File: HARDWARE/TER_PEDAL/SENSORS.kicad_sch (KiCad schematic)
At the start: 0 parts

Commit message: Added Sensors PSU
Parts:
- added C12 (x4): 10u, symbol Device:C
- added U3 (x2): LM1117MP-3.3, Package_TO_SOT_SMD:SOT-223-3_TabPin2, symbol Regulator_Linear:LM1117MP-3.3
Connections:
- new net: C12.1, U3.2 (VO) (x2)
- new net +5V: C12.1, C12.1, U3.3 (VI), U3.3 (VI)
- new net GND: C12.2, C12.2, C12.2, C12.2, U3.1 (GND), U3.1 (GND)

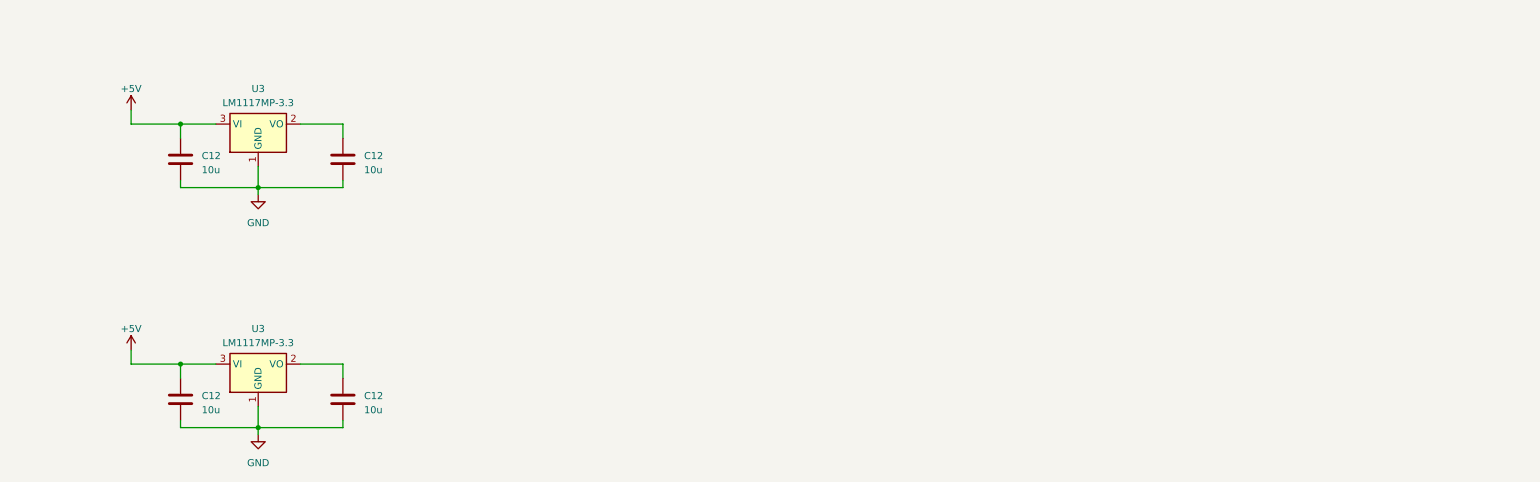
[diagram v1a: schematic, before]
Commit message: Added footprints to existing components
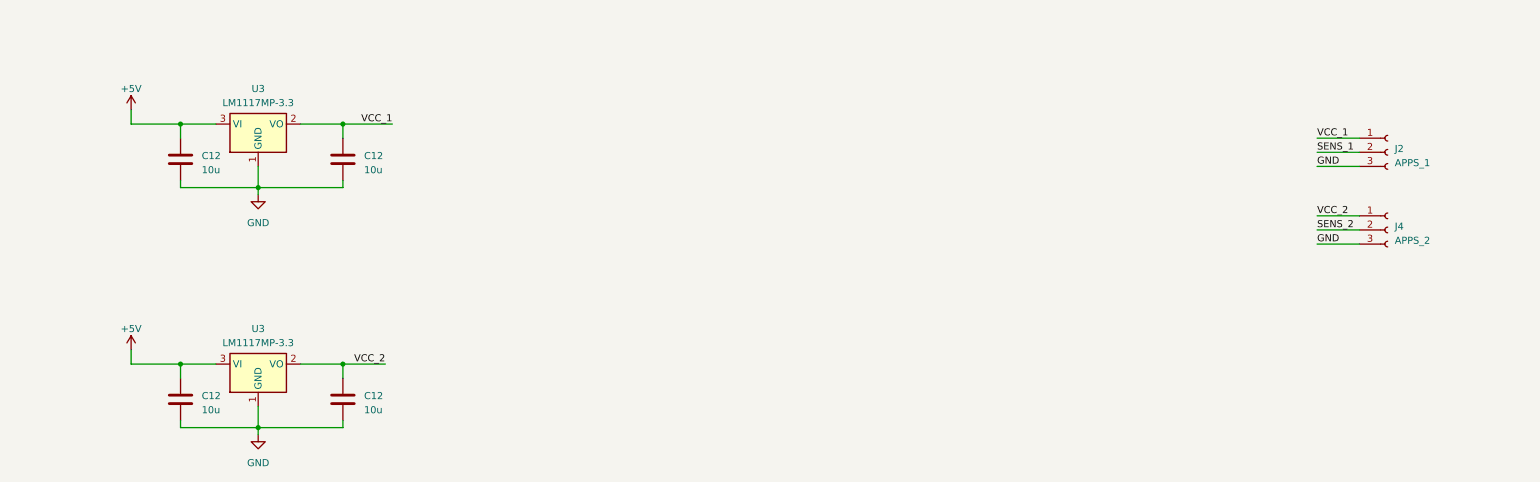
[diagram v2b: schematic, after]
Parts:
- added J2: APPS_1, Connector_Phoenix_MC:PhoenixContact_MCV_1,5_3-GF-3.5_1x03_P3.50mm_Vertical_ThreadedFlange_MountHole, symbol Connector:Conn_01x03_Female
- added J4: APPS_2, Connector_Phoenix_MC:PhoenixContact_MCV_1,5_3-GF-3.5_1x03_P3.50mm_Vertical_ThreadedFlange_MountHole, symbol Connector:Conn_01x03_Female
- C12: footprint (none) -> Capacitor_SMD:C_0603_1608Metric
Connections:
- net GND: now also J2.3 (Pin_3), J4.3 (Pin_3)
- net VCC_1: now reaches C12.1, U3.2 (VO)
- net VCC_1: now also J2.1 (Pin_1)
- net VCC_2: now reaches C12.1, U3.2 (VO)
- net VCC_2: now also J4.1 (Pin_1)
- new net SENS_1: J2.2 (Pin_2)
- new net SENS_2: J4.2 (Pin_2)
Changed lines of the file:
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@@
   (junction (at 41.91 33.02) (diameter 0) (color 0 0 0 0)
   )
+  (junction (at 71.12 76.2) (diameter 0) (color 0 0 0 0)
+  )
   (junction (at 41.91 76.2) (diameter 0) (color 0 0 0 0)
   )
   (junction (at 55.88 44.45) (diameter 0) (color 0 0 0 0)
   )
+  (junction (at 71.12 33.02) (diameter 0) (color 0 0 0 0)
+  )
   (junction (at 55.88 87.63) (diameter 0) (color 0 0 0 0)
   )
@@
     (stroke (width 0) (type default))
   )
+  (wire (pts (xy 246.38 35.56) (xy 254 35.56))
+    (stroke (width 0) (type default))
+  )
   (wire (pts (xy 41.91 76.2) (xy 33.02 76.2))
     (stroke (width 0) (type default))
@@
     (stroke (width 0) (type default))
   )
+  (wire (pts (xy 71.12 33.02) (xy 80.01 33.02))
+    (stroke (width 0) (type default))
+  )
   (wire (pts (xy 71.12 44.45) (xy 55.88 44.45))
     (stroke (width 0) (type default))
@@
     (stroke (width 0) (type default))
   )
+  (wire (pts (xy 246.38 54.61) (xy 254 54.61))
+    (stroke (width 0) (type default))
+  )
+  (wire (pts (xy 246.38 52.07) (xy 254 52.07))
+    (stroke (width 0) (type default))
+  )
+  (wire (pts (xy 246.38 40.64) (xy 254 40.64))
+    (stroke (width 0) (type default))
+  )
   (wire (pts (xy 41.91 86.36) (xy 41.91 87.63))
     (stroke (width 0) (type default))
@@
     (stroke (width 0) (type default))
   )
+  (wire (pts (xy 246.38 38.1) (xy 254 38.1))
+    (stroke (width 0) (type default))
+  )
   (wire (pts (xy 71.12 86.36) (xy 71.12 87.63))
     (stroke (width 0) (type default))
@@
     (stroke (width 0) (type default))
   )
+  (wire (pts (xy 71.12 76.2) (xy 78.74 76.2))
+    (stroke (width 0) (type default))
+  )
   (wire (pts (xy 63.5 76.2) (xy 71.12 76.2))
     (stroke (width 0) (type default))
   )
+  (wire (pts (xy 246.38 49.53) (xy 254 49.53))
+    (stroke (width 0) (type default))
+  )
   (wire (pts (xy 55.88 88.9) (xy 55.88 87.63))
     (stroke (width 0) (type default))
   )
+  (label "SENS_1" (at 246.38 38.1 0) (fields_autoplaced)
+    (effects (font (size 1.27 1.27)) (justify left bottom))
+  )
+  (label "VCC_2" (at 246.38 49.53 0) (fields_autoplaced)
+    (effects (font (size 1.27 1.27)) (justify left bottom))
+  )
+  (label "VCC_1" (at 246.38 35.56 0) (fields_autoplaced)
+    (effects (font (size 1.27 1.27)) (justify left bottom))
+  )
+  (label "VCC_2" (at 78.74 76.2 180) (fields_autoplaced)
+    (effects (font (size 1.27 1.27)) (justify right bottom))
+  )
+  (label "SENS_2" (at 246.38 52.07 0) (fields_autoplaced)
+    (effects (font (size 1.27 1.27)) (justify left bottom))
+  )
+  (label "GND" (at 246.38 54.61 0) (fields_autoplaced)
+    (effects (font (size 1.27 1.27)) (justify left bottom))
+  )
+  (label "VCC_1" (at 80.01 33.02 180) (fields_autoplaced)
+    (effects (font (size 1.27 1.27)) (justify right bottom))
+  )
+  (label "GND" (at 246.38 40.64 0) (fields_autoplaced)
+    (effects (font (size 1.27 1.27)) (justify left bottom))
+  )
   (symbol (lib_id "Device:C") (at 71.12 39.37 0) (unit 1)
     (in_bom yes) (on_board yes) (dnp no) (fields_autoplaced)
@@
       (effects (font (size 1.27 1.27)) (justify left))
     )
-    (property "Footprint" "" (at 72.0852 43.18 0)
+    (property "Footprint" "Capacitor_SMD:C_0603_1608Metric" (at 72.0852 43.18 0)
       (effects (font (size 1.27 1.27)) hide)
     )
@@
       (effects (font (size 1.27 1.27)) (justify left))
     )
-    (property "Footprint" "" (at 42.8752 86.36 0)
+    (property "Footprint" "Capacitor_SMD:C_0603_1608Metric" (at 42.8752 86.36 0)
       (effects (font (size 1.27 1.27)) hide)
     )
@@
       (effects (font (size 1.27 1.27)) (justify left))
     )
-    (property "Footprint" "" (at 72.0852 86.36 0)
+    (property "Footprint" "Capacitor_SMD:C_0603_1608Metric" (at 72.0852 86.36 0)
       (effects (font (size 1.27 1.27)) hide)
     )
@@
       (effects (font (size 1.27 1.27)) (justify left))
     )
-    (property "Footprint" "" (at 42.8752 43.18 0)
+    (property "Footprint" "Capacitor_SMD:C_0603_1608Metric" (at 42.8752 43.18 0)
       (effects (font (size 1.27 1.27)) hide)
     )
@@
         )
       )
+    )
+  )
+  (symbol (lib_id "Connector:Conn_01x03_Female") (at 259.08 38.1 0) (unit 1)
+    (in_bom yes) (on_board yes) (dnp no) (fields_autoplaced)
+    (property "Reference" "J2" (at 260.35 37.465 0)
+      (effects (font (size 1.27 1.27)) (justify left))
+    )
+    (property "Value" "APPS_1" (at 260.35 40.005 0)
+      (effects (font (size 1.27 1.27)) (justify left))
+    )
+    (property "Footprint" "Connector_Phoenix_MC:PhoenixContact_MCV_1,5_3-GF-3.5_1x03_P3.50mm_Vertical_ThreadedFlange_MountHole" (at 259.08 38.1 0)
+      (effects (font (size 1.27 1.27)) hide)
+    )
+    (property "Datasheet" "~" (at 259.08 38.1 0)
+      (effects (font (size 1.27 1.27)) hide)
+    )
+    (pin "1")
+    (pin "2")
+    (pin "3")
+    (instances
+      (project "TER_PEDAL"
+        (path "/73ede3a3-6344-40fe-9207-10ff50d388ba/bd370b0f-91e5-4328-9d6f-8dc10ff0cff7"
+          (reference "J2") (unit 1)
+        )
+      )
+    )
+  )
+  (symbol (lib_id "Connector:Conn_01x03_Female") (at 259.08 52.07 0) (unit 1)
+    (in_bom yes) (on_board yes) (dnp no) (fields_autoplaced)
+    (property "Reference" "J4" (at 260.35 51.435 0)
+      (effects (font (size 1.27 1.27)) (justify left))
+    )
+    (property "Value" "APPS_2" (at 260.35 53.975 0)
+      (effects (font (size 1.27 1.27)) (justify left))
+    )
+    (property "Footprint" "Connector_Phoenix_MC:PhoenixContact_MCV_1,5_3-GF-3.5_1x03_P3.50mm_Vertical_ThreadedFlange_MountHole" (at 259.08 52.07 0)
+      (effects (font (size 1.27 1.27)) hide)
+    )
+    (property "Datasheet" "~" (at 259.08 52.07 0)
+      (effects (font (size 1.27 1.27)) hide)
+    )
+    (pin "1")
+    (pin "2")
+    (pin "3")
+    (instances
+      (project "TER_PEDAL"
+        (path "/73ede3a3-6344-40fe-9207-10ff50d388ba/bd370b0f-91e5-4328-9d6f-8dc10ff0cff7"
+          (reference "J4") (unit 1)
+        )
+      )

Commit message: Finished Initial Schematic
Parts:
- added C23: 10u, Capacitor_SMD:C_0603_1608Metric, symbol Device:C_Small
- added J5: APPS_1, Connector_Phoenix_MC:PhoenixContact_MCV_1,5_3-GF-3.5_1x03_P3.50mm_Vertical_ThreadedFlange_MountHole, symbol Connector:Conn_01x03_Female
- added R10: 2k, Resistor_SMD:R_0603_1608Metric, symbol Device:R
- added R11: 4.7k, Resistor_SMD:R_0603_1608Metric, symbol Device:R
- added R12: 9.1k, Resistor_SMD:R_0603_1608Metric, symbol Device:R
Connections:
- net +5V: now also C23.1, J5.1 (Pin_1)
- net GND: now also C23.2, J5.3 (Pin_3), R12.2
- net SENS_2: now also R10.2
- net SENS_1 renamed APPS_1
- new net APPS_2: R10.1
- new net BPPS: R11.2, R12.1
- new net Brake: J5.2 (Pin_2), R11.1
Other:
- note added: "5v -> 3v signal sifter"
- note added: "APPS Connections"
- note added: "Brake Pedal Position Sensor BPPS"
- note added: "Este resistor está para inclinar la función de transferencia del APPS_2 y que no coincida con la del APPS_1 cambiar por un 0R si se quiere hacer bypass"
- note added: "Independent APPS PSU"
- moved on the sheet: C12, J2, J4, U3

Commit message: Started Layout and fixed wrong footprints
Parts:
- J2, J4: footprint Connector_Phoenix_MC:PhoenixContact_MCV_1,5_3-GF-3.5_1x03_P3.50mm_Vertical_ThreadedFlange_MountHole -> Connector_Wuerth:Wuerth_WR-WTB_64800311622_1x03_P1.50mm_Vertical
- J5: value APPS_1 -> BPPS_1; footprint Connector_Phoenix_MC:PhoenixContact_MCV_1,5_3-GF-3.5_1x03_P3.50mm_Vertical_ThreadedFlange_MountHole -> Connector_Wuerth:Wuerth_WR-WTB_64800311622_1x03_P1.50mm_Vertical
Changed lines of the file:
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@@
       (effects (font (size 1.27 1.27)) (justify left))
     )
-    (property "Footprint" "Connector_Phoenix_MC:PhoenixContact_MCV_1,5_3-GF-3.5_1x03_P3.50mm_Vertical_ThreadedFlange_MountHole" (at 166.37 34.29 0)
+    (property "Footprint" "Connector_Wuerth:Wuerth_WR-WTB_64800311622_1x03_P1.50mm_Vertical" (at 166.37 34.29 0)
       (effects (font (size 1.27 1.27)) hide)
     )
@@
       (effects (font (size 1.27 1.27)) (justify left))
     )
-    (property "Footprint" "Connector_Phoenix_MC:PhoenixContact_MCV_1,5_3-GF-3.5_1x03_P3.50mm_Vertical_ThreadedFlange_MountHole" (at 166.37 48.26 0)
+    (property "Footprint" "Connector_Wuerth:Wuerth_WR-WTB_64800311622_1x03_P1.50mm_Vertical" (at 166.37 48.26 0)
       (effects (font (size 1.27 1.27)) hide)
     )
@@
       (effects (font (size 1.27 1.27)) (justify left))
     )
-    (property "Value" "APPS_1" (at 273.05 48.895 0)
+    (property "Value" "BPPS_1" (at 273.05 48.895 0)
       (effects (font (size 1.27 1.27)) (justify left))
     )
-    (property "Footprint" "Connector_Phoenix_MC:PhoenixContact_MCV_1,5_3-GF-3.5_1x03_P3.50mm_Vertical_ThreadedFlange_MountHole" (at 271.78 46.99 0)
+    (property "Footprint" "Connector_Wuerth:Wuerth_WR-WTB_64800311622_1x03_P1.50mm_Vertical" (at 271.78 46.99 0)
       (effects (font (size 1.27 1.27)) hide)
     )

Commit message: Added Eracing Logo
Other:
- note added: "Brake Pedal Pressure Sensor BPPS"
- note removed: "Brake Pedal Position Sensor BPPS"
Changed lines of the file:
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@@
     (effects (font (size 2 2) (thickness 0.4) bold) (justify left bottom))
   )
-  (text "Brake Pedal Position Sensor BPPS" (at 184.15 17.78 0)
+  (text "Brake Pedal Pressure Sensor BPPS" (at 184.15 17.78 0)
     (effects (font (size 2 2) (thickness 0.4) bold) (justify left bottom))
   )

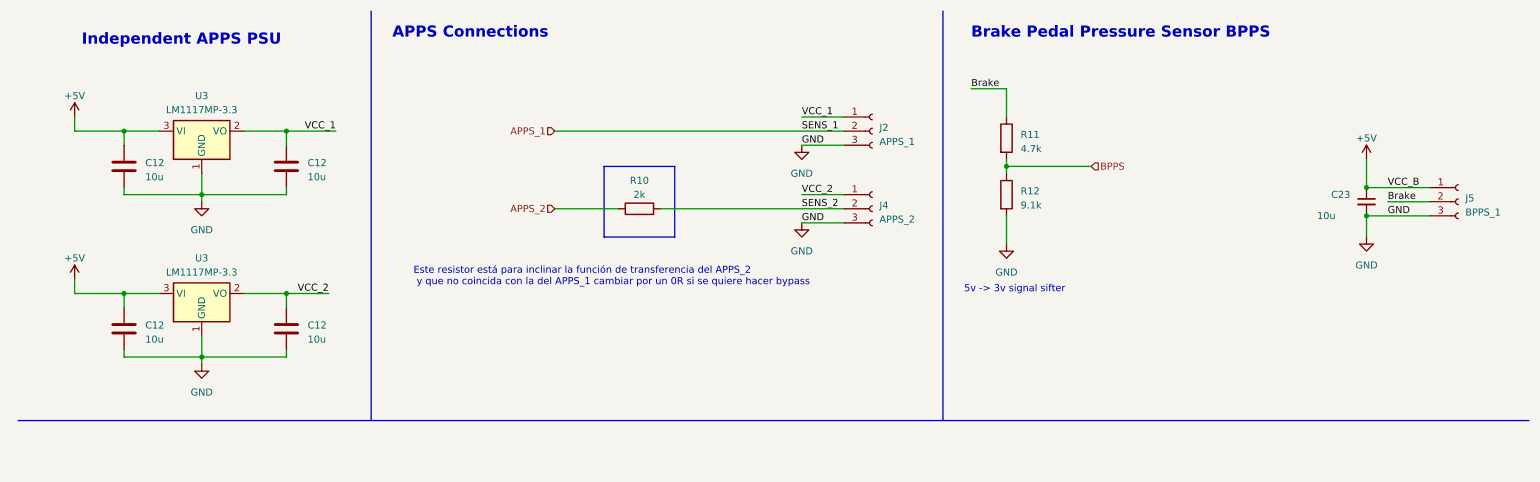
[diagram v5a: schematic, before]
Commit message: Added decouple to all sensors and a new steering sensor input
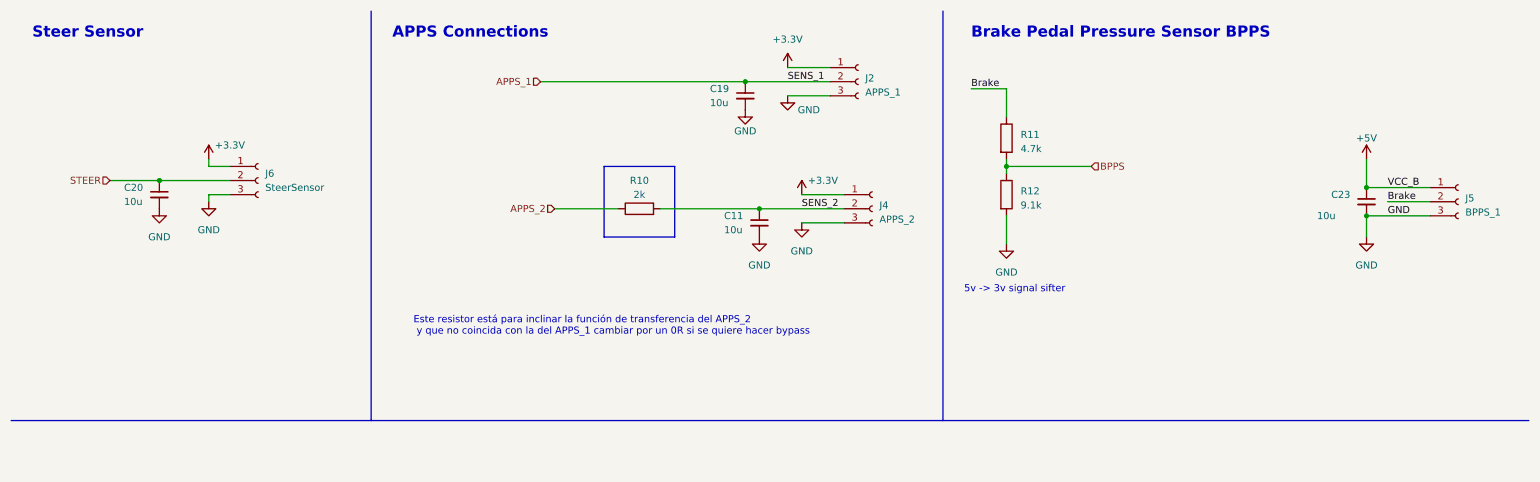
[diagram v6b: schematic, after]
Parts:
- removed C12 (x4): 10u, Capacitor_SMD:C_0603_1608Metric, symbol Device:C
- removed U3 (x2): LM1117MP-3.3, Package_TO_SOT_SMD:SOT-223-3_TabPin2, symbol Regulator_Linear:LM1117MP-3.3
- added C11, C19, C20: 10u, Capacitor_SMD:C_0603_1608Metric, symbol Device:C_Small
- added J6: SteerSensor, Connector_Wuerth:Wuerth_WR-WTB_64800311622_1x03_P1.50mm_Vertical, symbol Connector:Conn_01x03_Female
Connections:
- net VCC_2 is gone; now on net +3.3V: J4.1 (Pin_1)
- net APPS_1: now also C19.1
- net GND: now also C11.2, C19.2, C20.2, J6.3 (Pin_3)
- net SENS_2: now also C11.1
- net VCC_1 renamed +3.3V
- net +3.3V: now also J6.1 (Pin_1)
- new net STEER: C20.1, J6.2 (Pin_2)
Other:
- note added: "Steer Sensor"
- note removed: "Independent APPS PSU"
- moved on the sheet: J2

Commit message: Rearranged board
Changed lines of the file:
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@@
       (effects (font (size 1.27 1.27)) (justify left))
     )
-    (property "Value" "10u" (at 246.38 49.53 0)
+    (property "Value" "10u" (at 248.92 49.53 0)
       (effects (font (size 1.27 1.27)) (justify left))
     )

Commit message: Added holes, connectors and finished re-layout
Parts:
- J2, J4, J5, J6: footprint Connector_Wuerth:Wuerth_WR-WTB_64800311622_1x03_P1.50mm_Vertical -> Connector_JST:JST_PH_S3B-PH-K_1x03_P2.00mm_Horizontal
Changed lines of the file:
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@@
       (effects (font (size 1.27 1.27)) (justify left))
     )
-    (property "Footprint" "Connector_Wuerth:Wuerth_WR-WTB_64800311622_1x03_P1.50mm_Vertical" (at 55.88 43.18 0)
+    (property "Footprint" "Connector_JST:JST_PH_S3B-PH-K_1x03_P2.00mm_Horizontal" (at 55.88 43.18 0)
       (effects (font (size 1.27 1.27)) hide)
     )
@@
       (effects (font (size 1.27 1.27)) (justify left))
     )
-    (property "Footprint" "Connector_Wuerth:Wuerth_WR-WTB_64800311622_1x03_P1.50mm_Vertical" (at 163.83 25.4 0)
+    (property "Footprint" "Connector_JST:JST_PH_S3B-PH-K_1x03_P2.00mm_Horizontal" (at 163.83 25.4 0)
       (effects (font (size 1.27 1.27)) hide)
     )
@@
       (effects (font (size 1.27 1.27)) (justify left))
     )
-    (property "Footprint" "Connector_Wuerth:Wuerth_WR-WTB_64800311622_1x03_P1.50mm_Vertical" (at 166.37 48.26 0)
+    (property "Footprint" "Connector_JST:JST_PH_S3B-PH-K_1x03_P2.00mm_Horizontal" (at 166.37 48.26 0)
       (effects (font (size 1.27 1.27)) hide)
     )
@@
       (effects (font (size 1.27 1.27)) (justify left))
     )
-    (property "Footprint" "Connector_Wuerth:Wuerth_WR-WTB_64800311622_1x03_P1.50mm_Vertical" (at 271.78 46.99 0)
-      (effects (font (size 1.27 1.27)) hide)
-    )
+    (property "Footprint" "Connector_JST:JST_PH_S3B-PH-K_1x03_P2.00mm_Horizontal" (at 271.78 46.99 0)
+      (effects (font (size 1.27 1.27)) hide)
+    )
